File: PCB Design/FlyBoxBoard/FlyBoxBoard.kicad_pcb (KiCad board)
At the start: 2 copper layers, 148.6 x 119.4 mm, 42 parts, among them J1 5V in, J10 RED, J11 GREEN, J12 WHITE, J13 INFRARED, J14 LCD, J15 SD card reader, J16 5K Ohms, J17 5K Ohms, J18 ESP 32 Left Side extra pins, J19 ESP 32 Left Side extra pinouts, J2 12V in, J20 Transistor, J21 Logic Level LV pinouts, J22 Potentiometer, J23 Logic Level Left Side LV, J24 ESP 32 Right Side extra pinou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, J25 ESP 32 Right Side extra pinou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, J26 BuckPuck IR, J27 Logic Level Right Side HV, J28 Logic Level HV pins, J29 5K Ohms, J3 ESP 32 Left Side, J30 5K Ohms, J31 5K Ohms, J32 5K Ohms, J33 5K Ohms, J34 5K Ohms, J35 Transistor, J36 Transistor, J37 Transistor, J38 BuckPuck White, J39 BuckPuck Green, J4 Real Time Controller, J40 BuckPuck Red, J5 ESP 32 Right Side, J9 FAN

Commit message: 3/1 updates
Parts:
- added J22: Potentiometer, Connector_PinSocket_2.54mm:PinSocket_1x05_P2.54mm_Vertical, F.Cu at (134.6, 120.7)
- J1, J10, J11, J12, J13, J2: footprint Connector_PinSocket_2.54mm:PinSocket_1x02_P2.54mm_Vertical -> TerminalBlock:TerminalBlock_bornier-2_P5.08mm
- J14: value LCD -> LCD Screen
- J18: value ESP 32 Left Side extra pins -> ESP 32 Left Side extra pinouts
- J21: value Logic Level LV pinouts -> Logic Level LV pins
- J22: footprint Connector_PinSocket_2.54mm:PinSocket_1x03_P2.54mm_Vertical -> Connector_PinSocket_2.54mm:PinSocket_1x05_P2.54mm_Vertical
- J9: value FAN -> FANS
- moved G*** 136.9 mm to (34.3, 38.1)
- moved J4 39.6 mm to (68.6, 63.5)
- moved G*** 15.4 mm to (33.7, 30.5), turned to 0 degrees
- moved J22 15.2 mm to (139.7, 120.7)
- moved J12 13.5 mm to (95.2, 24.8), turned to 180 degrees
- moved J11 12.2 mm to (82.5, 24.8), turned to 180 degrees
- moved J10 9.09 mm to (69.8, 24.8), turned to 180 degrees
- moved J2 6.25 mm to (114.3, 26.0), turned to 90 degrees
- moved J13 6.02 mm to (57.1, 24.8), turned to 180 degrees
- moved J39 5.61 mm to (144.8, 53.3)
- moved J26 5.59 mm to (144.8, 96.5)
- moved J40 4.55 mm to (144.8, 74.9)
- moved J38 4.34 mm to (144.8, 31.8)
- moved J8 2.52 mm to (94.0, 44.5)
- moved J1 0.90 mm to (134.0, 21.0), turned to -90 degrees
- renumbered 5V to J6, 12V to J7, GND to J8
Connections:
- J16 pad 5: Net-(J20-Pad3) -> Net-(J16-Pad5)
- J20 pad 3: Net-(J20-Pad3) -> Net-(J16-Pad5)
- J22 pad 2: Net-(J20-Pad3) -> unconnected-(J22-Pad2)
- J22 pad 3: Net-(J20-Pad3) -> Net-(J20-Pad1)
- J26 pad 4: Net-(J20-Pad3) -> Net-(J16-Pad5)
- J4 pad 3: /D22 -> /D21
- J4 pad 4: /D21 -> /D22
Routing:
- net Net-(J16-Pad5): track 0.00 -> 64.7 mm
- net Net-(J20-Pad1): track 15.8 -> 50.4 mm
- net Net-(J20-Pad3): track 27.7 -> 0.00 mm
- net /5V: track 340.3 -> 321.2 mm
- net /W LED+: track 70.2 -> 52.4 mm
- net /G LED+: track 92.2 -> 76.7 mm
- net /W LED-: track 73.8 -> 60.4 mm
- net /G LED-: track 95.6 -> 82.8 mm
- net /D21: track 120.4 -> 127.9 mm, vias 4 -> 6
- net /IR LED+: track 152.4 -> 145.6 mm
- net /R LED+: track 122.3 -> 116.4 mm
- net /12V: track 278.9 -> 274.4 mm
- net /IR LED-: track 156.6 -> 152.1 mm
- net /D22: track 126.1 -> 129.1 mm, vias 4 -> 6
- net /3V3: track 169.5 -> 172.2 mm
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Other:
- board text added: "- +"
- board text added: "GND"

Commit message: 3/1 Changes pt 2
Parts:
- J9: footprint Connector_PinSocket_2.54mm:PinSocket_1x04_P2.54mm_Vertical -> TerminalBlock:TerminalBlock_bornier-4_P5.08mm
- moved J9 10.3 mm to (45.7, 24.8), turned to 180 degrees
- moved G*** 7.10 mm to (35.6, 45.1)
- moved G*** 6.99 mm to (33.7, 37.5)
- moved J10 1.27 mm to (71.1, 24.8)
- moved J13 1.27 mm to (58.4, 24.8)
- moved J11 1.27 mm to (83.8, 24.8)
- moved J12 1.27 mm to (96.5, 24.8)
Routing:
- net /HV5: track 117.1 -> 111.0 mm
- net /12V: track 274.4 -> 280.3 mm
- net /R LED-: track 124.3 -> 124.8 mm
- net /IR LED+: track 145.6 -> 146.2 mm
- net /R LED+: track 116.4 -> 116.9 mm
- net /W LED+: track 52.4 -> 51.9 mm
- net /IR LED-: track 152.1 -> 152.6 mm
- net /G LED-: track 82.8 -> 83.3 mm
- net /W LED-: track 60.4 -> 60.9 mm
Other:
- outline, holes or cut-outs redrawn
- board text added: "GND 12V SIG"
- board text added: "GND 5V SDA SCL"
- board text added: "GND Miso SCK Mosi CS 3V3"

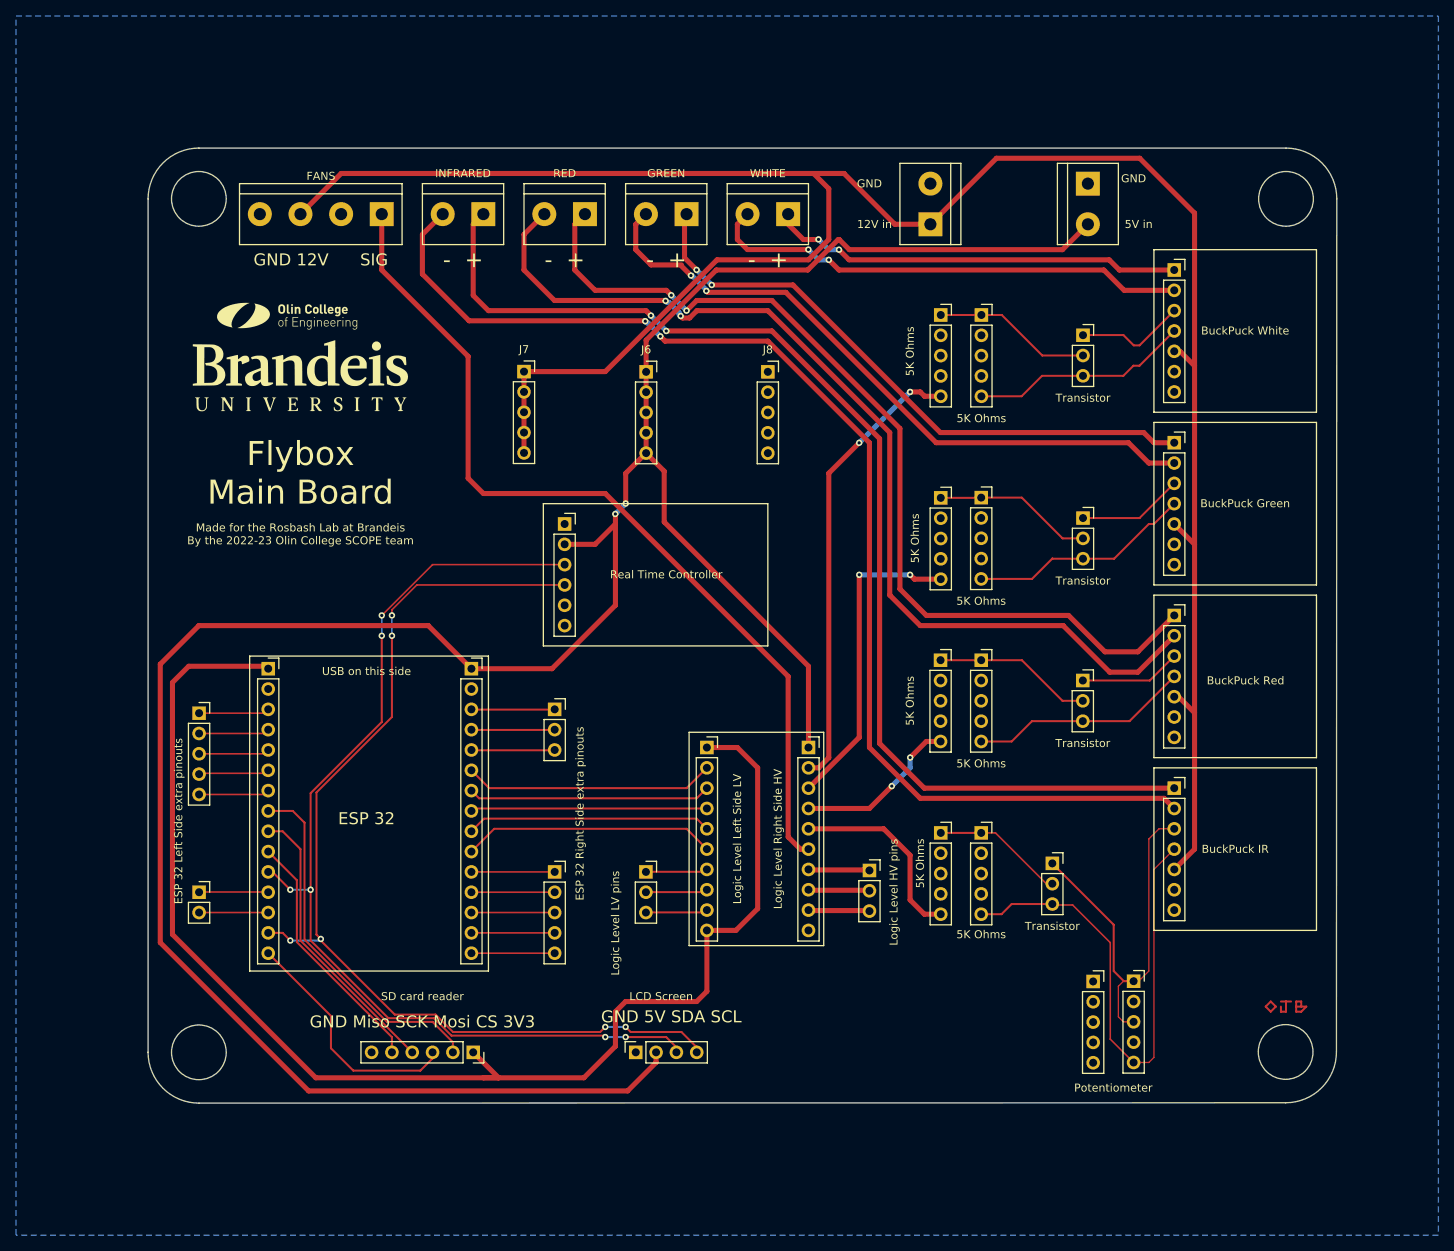
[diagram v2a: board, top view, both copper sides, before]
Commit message: 3/8 Work
Missing button footprint
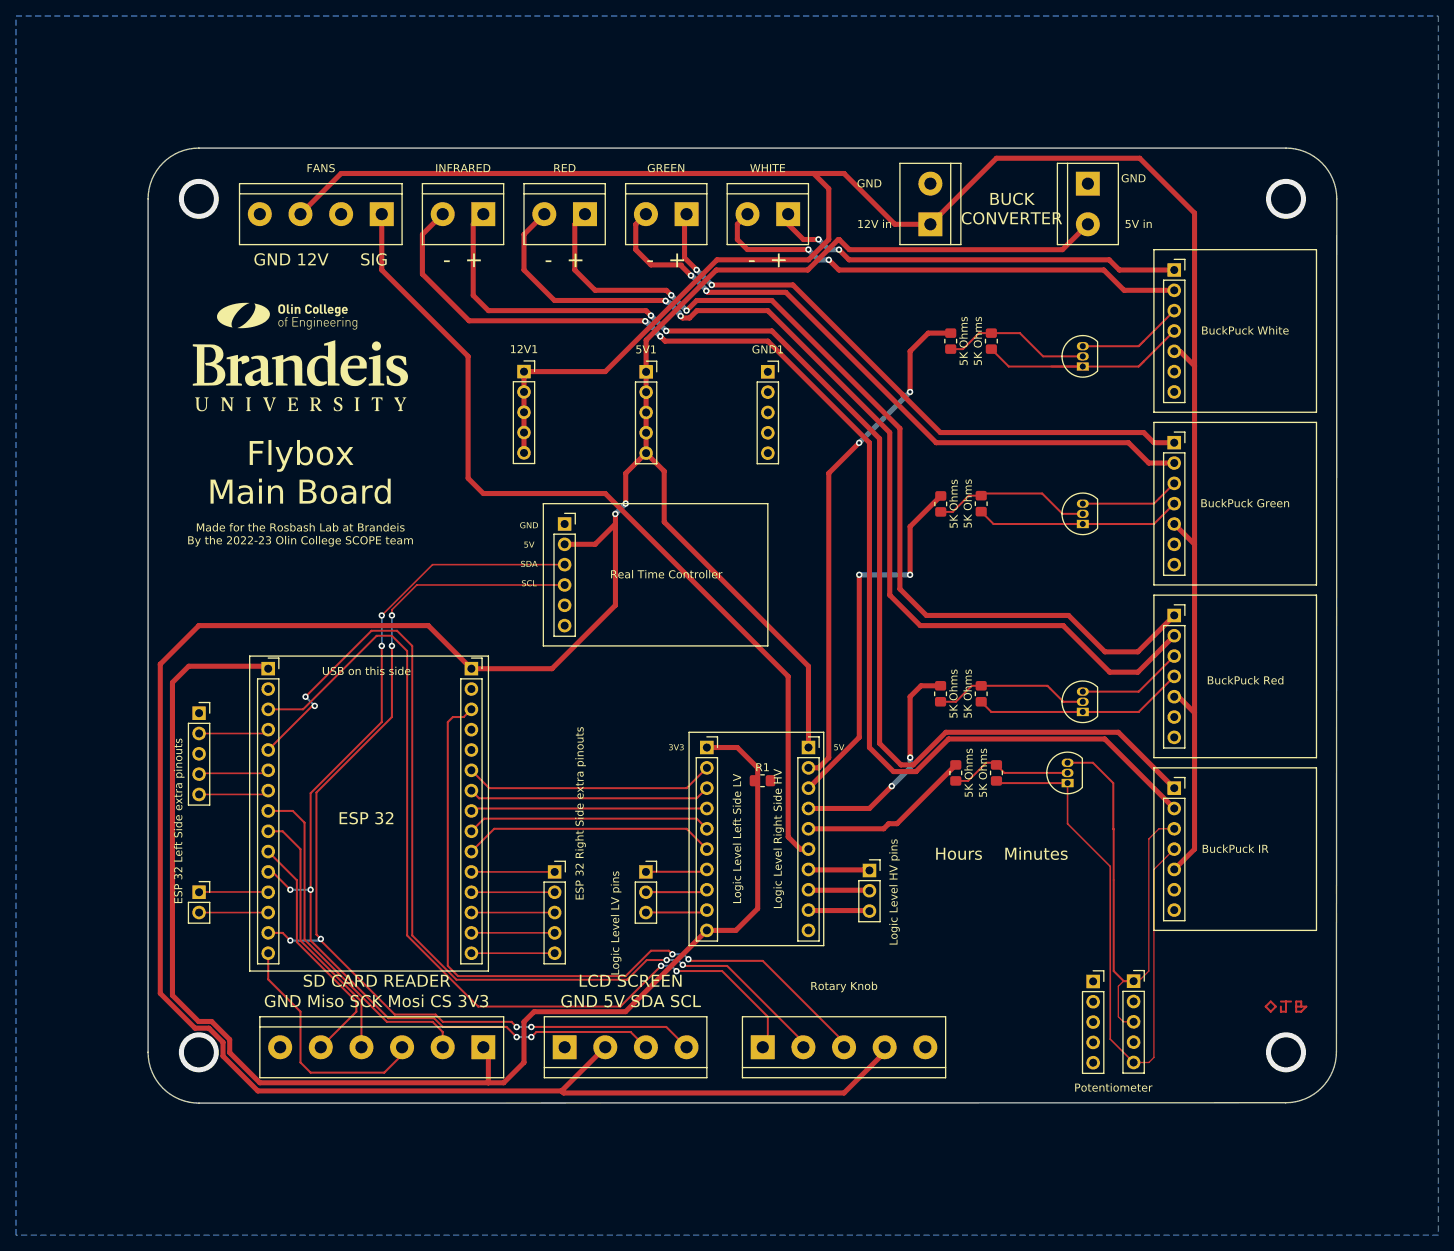
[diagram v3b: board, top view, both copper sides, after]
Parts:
- removed J24: ESP 32 Right Side extra pinouts, Connector_PinSocket_2.54mm:PinSocket_1x03_P2.54mm_Vertical
- added J6: Rotary Knob, TerminalBlock:TerminalBlock_bornier-5_P5.08mm, F.Cu at (93.3, 128.9)
- added R1: R_US, Resistor_SMD:R_0805_2012Metric_Pad1.20x1.40mm_HandSolder, F.Cu at (93.3, 95.6)
- J14: footprint Connector_PinSocket_2.54mm:PinSocket_1x04_P2.54mm_Vertical -> TerminalBlock:TerminalBlock_bornier-4_P5.08mm
- J15: footprint Connector_PinSocket_2.54mm:PinSocket_1x06_P2.54mm_Vertical -> TerminalBlock:TerminalBlock_bornier-6_P5.08mm
- J16, J17, J29, J30, J31, J32, J33, J34: footprint Connector_PinSocket_2.54mm:PinSocket_1x05_P2.54mm_Vertical -> Resistor_SMD:R_0805_2012Metric_Pad1.20x1.40mm_HandSolder
- J20, J35, J36, J37: footprint Connector_PinSocket_2.54mm:PinSocket_1x03_P2.54mm_Vertical -> Package_TO_SOT_THT:TO-92_Inline
- moved J20 10.2 mm to (131.4, 95.9), turned to 90 degrees
- moved J14 8.91 mm to (68.6, 128.9), turned to 0 degrees
- moved J16 7.74 mm to (122.6, 94.6), turned to -90 degrees
- moved J17 7.73 mm to (117.5, 94.6), turned to 90 degrees
- moved J33 4.20 mm to (120.7, 84.7), turned to -90 degrees
- moved J34 4.20 mm to (115.6, 84.7), turned to 90 degrees
- moved J37 3.93 mm to (133.3, 87.0), turned to 90 degrees
- moved J35 3.92 mm to (133.3, 43.8), turned to 90 degrees
- moved J29 3.50 mm to (121.9, 40.6), turned to -90 degrees
- moved J30 3.50 mm to (116.8, 40.6), turned to 90 degrees
- moved J15 1.42 mm to (58.4, 128.9), turned to 180 degrees
- moved J31 0.76 mm to (120.7, 61.0), turned to -90 degrees
- moved J32 0.76 mm to (115.6, 61.0), turned to 90 degrees
- moved J36 0.74 mm to (133.3, 63.5), turned to 90 degrees
- renumbered J7 to 12V1, J6 to 5V1, J8 to GND1
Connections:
- J16 pad 2: unconnected-(J16-Pad2) -> Net-(J20-Pad1)
- J17 pad 2: unconnected-(J17-Pad2) -> /HV4
- J18 pad 1: Net-(J18-Pad1) -> unconnected-(J18-Pad1)
- J18 pad 3: Net-(J18-Pad3) -> unconnected-(J18-Pad3)
- J20 pad 3: Net-(J16-Pad5) -> Net-(J22-Pad1)
- J22 pad 1: Net-(J20-Pad1) -> Net-(J22-Pad1)
- J22 pad 3: Net-(J20-Pad1) -> Net-(J22-Pad1)
- J22 pad 5: Net-(J16-Pad5) -> Net-(J20-Pad1)
- J26 pad 3: Net-(J20-Pad1) -> Net-(J22-Pad1)
- J26 pad 4: Net-(J16-Pad5) -> Net-(J20-Pad1)
- J29 pad 2: unconnected-(J29-Pad2) -> Net-(J29-Pad2)
- J3 pad 3: Net-(J18-Pad1) -> /D15
- J3 pad 5: Net-(J18-Pad3) -> /D4
- J30 pad 2: unconnected-(J30-Pad2) -> /HV1
- J31 pad 2: unconnected-(J31-Pad2) -> Net-(J31-Pad2)
- J32 pad 2: unconnected-(J32-Pad2) -> /HV2
- J33 pad 2: unconnected-(J33-Pad2) -> Net-(J37-Pad1)
- J34 pad 2: unconnected-(J34-Pad2) -> /HV3
- J35 pad 1: Net-(J35-Pad1) -> Net-(J29-Pad2)
- J35 pad 3: Net-(J29-Pad5) -> Net-(J38-Pad3)
- J36 pad 1: Net-(J36-Pad1) -> Net-(J31-Pad2)
- J36 pad 3: Net-(J31-Pad5) -> Net-(J39-Pad3)
- J37 pad 3: Net-(J33-Pad5) -> Net-(J40-Pad3)
- J38 pad 3: Net-(J35-Pad1) -> Net-(J38-Pad3)
- J38 pad 4: Net-(J29-Pad5) -> Net-(J29-Pad2)
- J39 pad 3: Net-(J36-Pad1) -> Net-(J39-Pad3)
- J39 pad 4: Net-(J31-Pad5) -> Net-(J31-Pad2)
- J40 pad 3: Net-(J37-Pad1) -> Net-(J40-Pad3)
- J40 pad 4: Net-(J33-Pad5) -> Net-(J37-Pad1)
- J5 pad 3: Net-(J24-Pad1) -> /D13
- J5 pad 4: Net-(J24-Pad2) -> /D12
- J5 pad 5: Net-(J24-Pad3) -> /D14
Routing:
- net /D4: track 0.00 -> 120.7 mm, vias 0 -> 4
- net /D15: track 0.00 -> 115.3 mm, vias 0 -> 2
- net /D13: track 0.00 -> 90.9 mm, vias 0 -> 2
- net Net-(J16-Pad5): track 64.7 -> 0.00 mm
- net Net-(J22-Pad1): track 0.00 -> 64.1 mm
- net /5V: track 321.2 -> 362.4 mm
- net Net-(J29-Pad2): track 0.00 -> 30.3 mm
- net Net-(J31-Pad5): track 28.0 -> 0.00 mm
- net Net-(J33-Pad5): track 28.0 -> 0.00 mm
- net Net-(J29-Pad5): track 27.5 -> 0.00 mm
- net Net-(J20-Pad1): track 50.4 -> 77.2 mm
- net Net-(J31-Pad2): track 0.00 -> 25.8 mm
- net Net-(J38-Pad3): track 0.00 -> 14.0 mm
- net Net-(J37-Pad1): track 12.7 -> 26.5 mm
- net Net-(J35-Pad1): track 13.8 -> 0.00 mm
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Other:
- outline, holes or cut-outs redrawn
- board text added: "3V3"
- board text added: "5V"
- board text added: "BUCK CONVERTER"
- board text added: "Hours Minutes"
- board text added: "LCD SCREEN"
- board text added: "SD CARD READER"

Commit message: V2 IR and RGW boards done
Main board missing button footprint
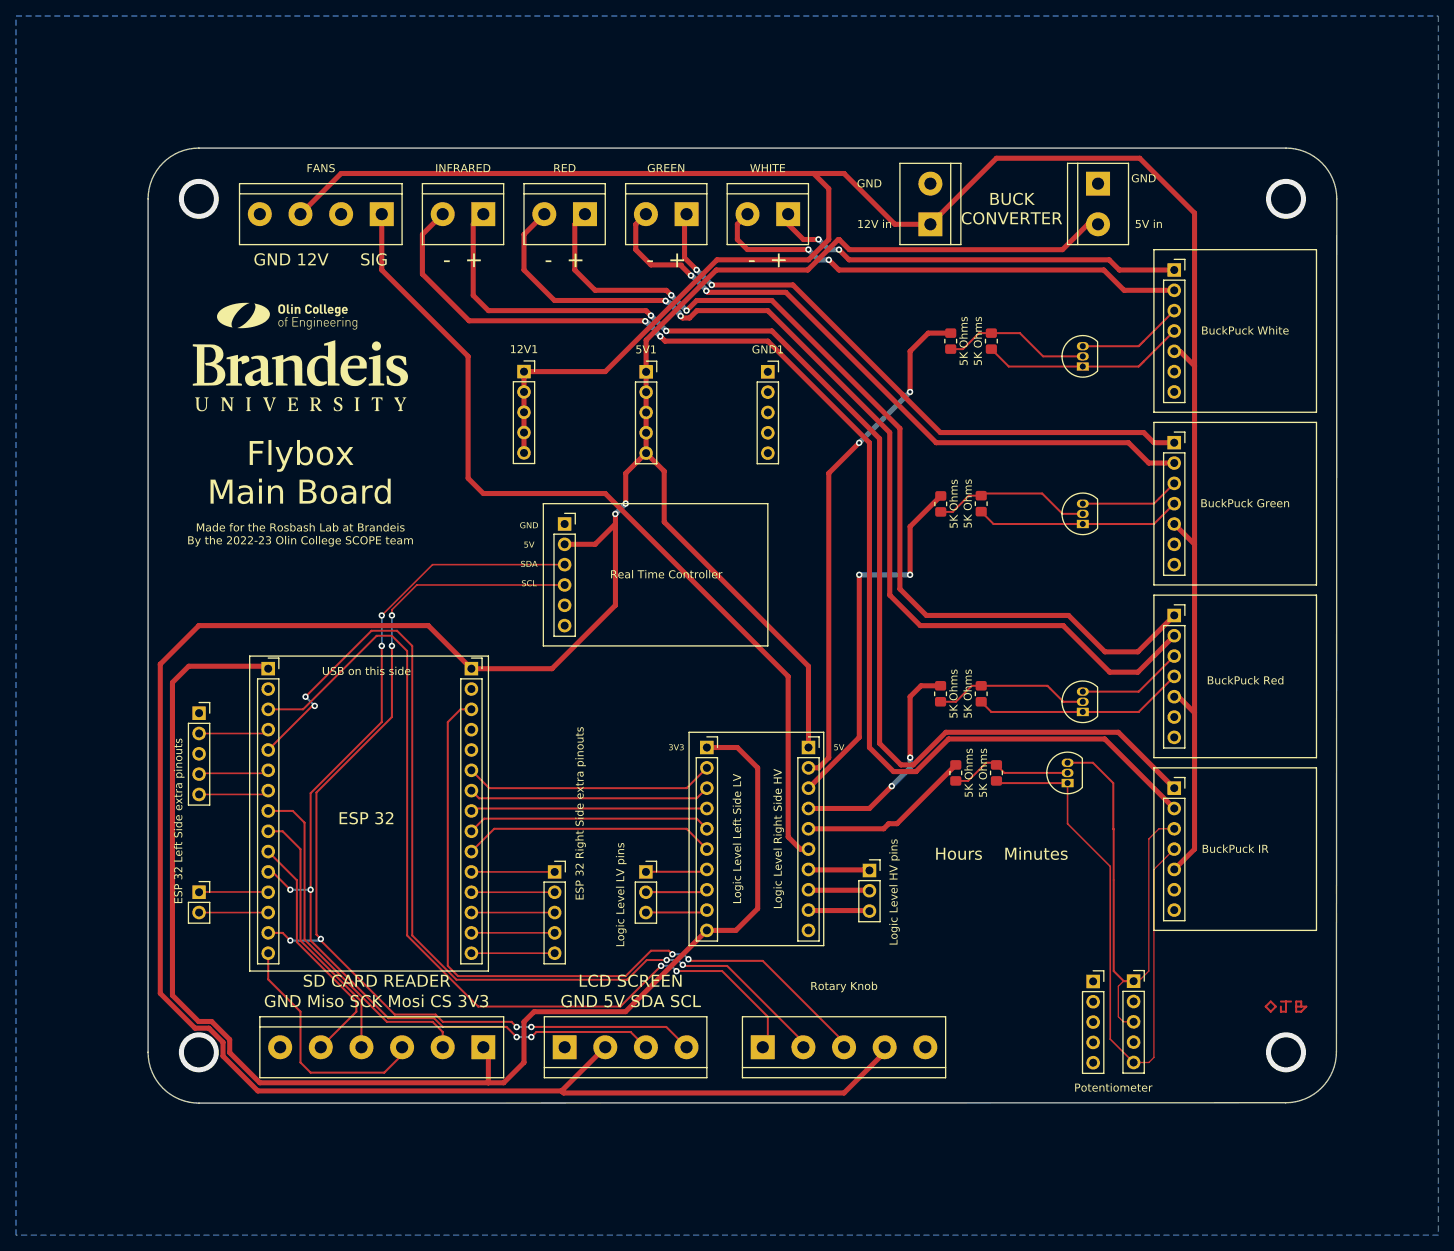
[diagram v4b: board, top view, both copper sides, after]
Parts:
- removed R1: R_US, Resistor_SMD:R_0805_2012Metric_Pad1.20x1.40mm_HandSolder
- moved J1 1.27 mm to (135.3, 21.0)
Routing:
- net Net-(J29-Pad2): track 30.3 -> 26.4 mm
- net /5V: track 362.4 -> 363.6 mm
- net /GND: vias 0 -> 4
- net (no net): vias 4 -> 0
